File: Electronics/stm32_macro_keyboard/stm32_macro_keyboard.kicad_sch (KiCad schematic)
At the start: 26 parts, among them SW1 SW_SPDT, U1 STM32F072CBTx

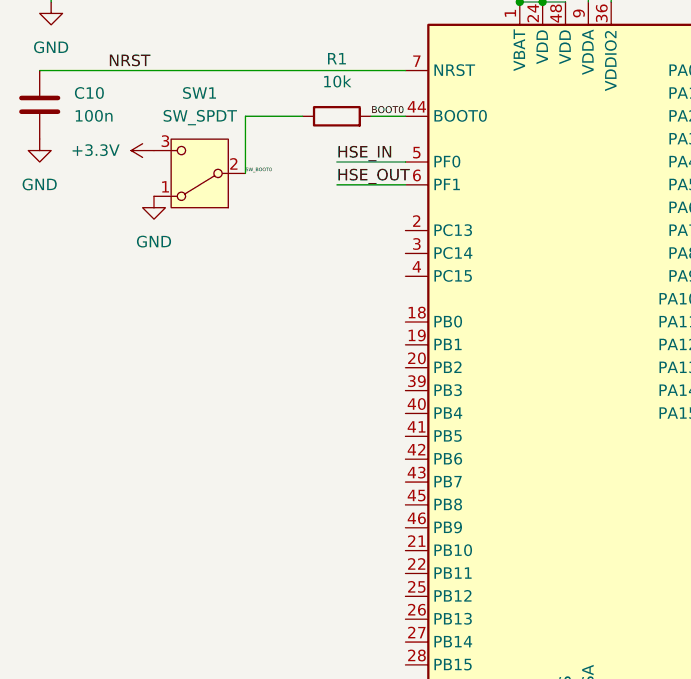
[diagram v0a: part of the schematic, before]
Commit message: Add 16 MHz HSE crystal oscillator circuit
- Add Y1 (Crystal_GND24) 16 MHz crystal on PF0/PF1 (HSE_IN/HSE_OUT)
- Add C11 and C12 (10pF) load capacitors for crystal oscillator
- Add GND connection for crystal ground pins
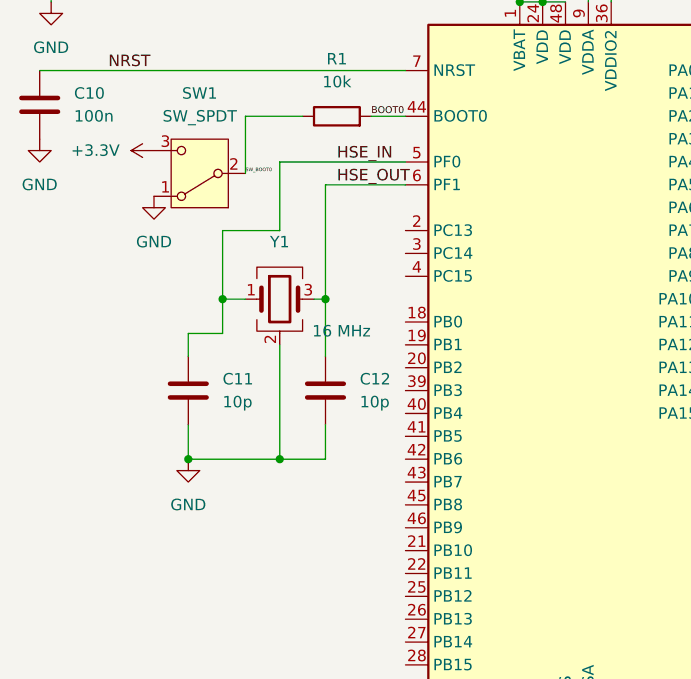
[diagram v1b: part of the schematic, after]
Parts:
- added C11, C12: 10p, symbol Device:C
- added Y1: 16 MHz, symbol Device:Crystal_GND24
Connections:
- net GND: now also C11.2, C12.2, Y1.2 (G), Y1.4 (G)
- net HSE_IN: now also C11.1, Y1.1
- net HSE_OUT: now also C12.1, Y1.3

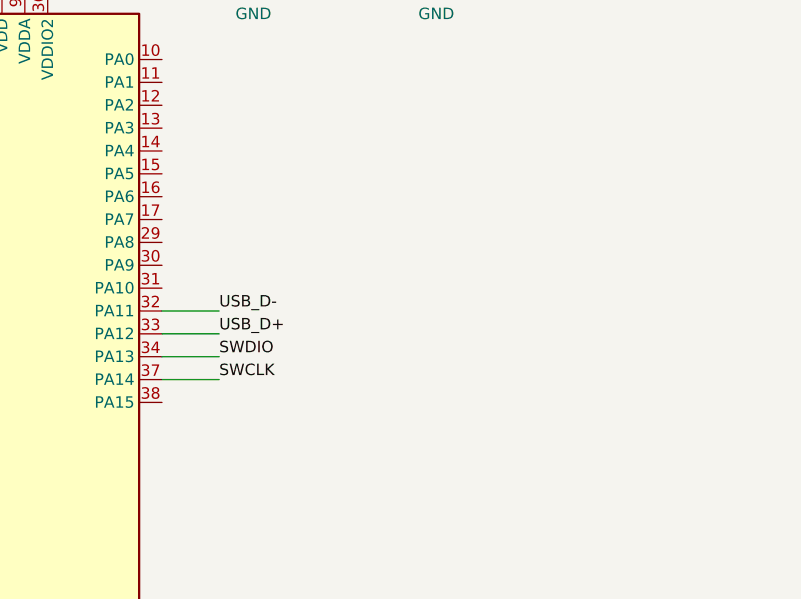
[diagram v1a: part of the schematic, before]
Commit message: Add USB Micro B connector (J1) with power and data connections
- Add J1 (USB_B_Micro) connector symbol
- Connect D- and D+ to USB_D-/USB_D+ nets on PA11/PA12
- Connect VBUS to VBUS power rail and GND pin to GND
- Mark ID and Shield pins as no-connect
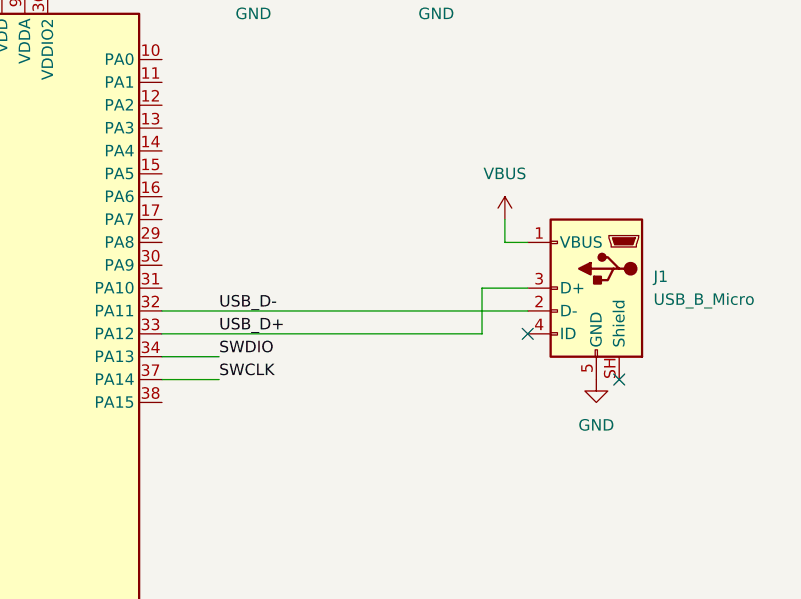
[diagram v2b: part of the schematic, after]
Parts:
- added J1: USB_B_Micro, symbol Connector:USB_B_Micro
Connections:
- net GND: now also J1.5 (GND)
- net USB_D+: now also J1.3 (D+)
- net USB_D-: now also J1.2 (D-)
- new net VBUS: J1.1 (VBUS)
- no-connect marks 0 -> 2

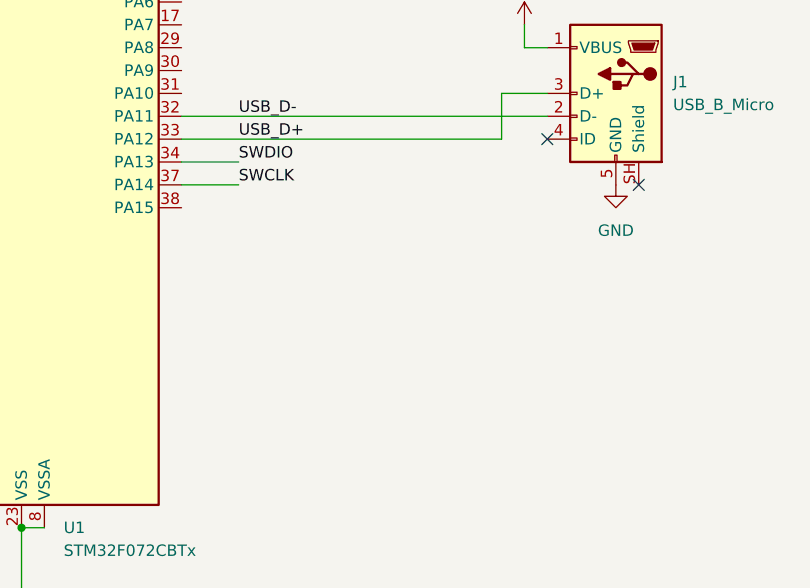
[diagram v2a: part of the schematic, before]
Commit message: Add SWD debug header (J2) and power symbols to schematic
Add a 4-pin connector J2 for SWD debug access with +3.3V and GND power
symbols. Route MCU SWD signals (SWDIO/SWCLK) to the new header via wires.
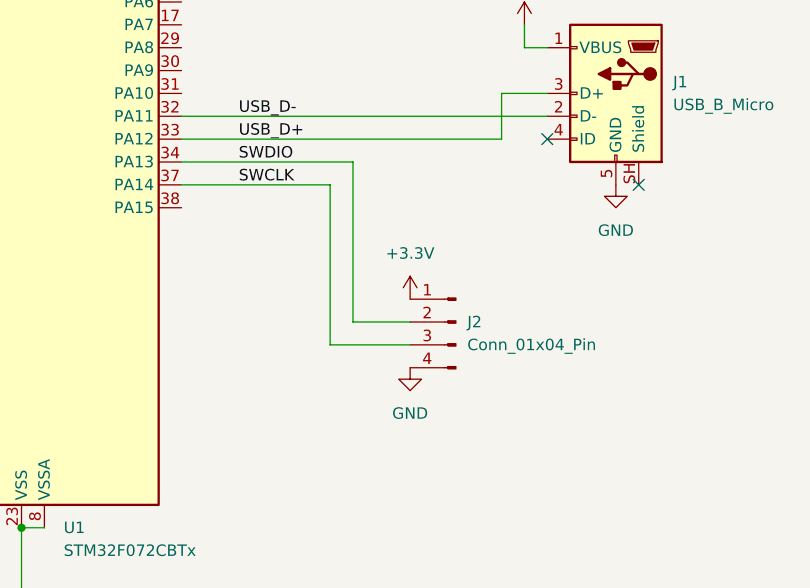
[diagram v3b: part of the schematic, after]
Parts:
- added J2: Conn_01x04_Pin, symbol Connector:Conn_01x04_Pin
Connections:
- net +3.3V: now also J2.1 (Pin_1)
- net GND: now also J2.4 (Pin_4)
- net SWCLK: now also J2.3 (Pin_3)
- net SWDIO: now also J2.2 (Pin_2)

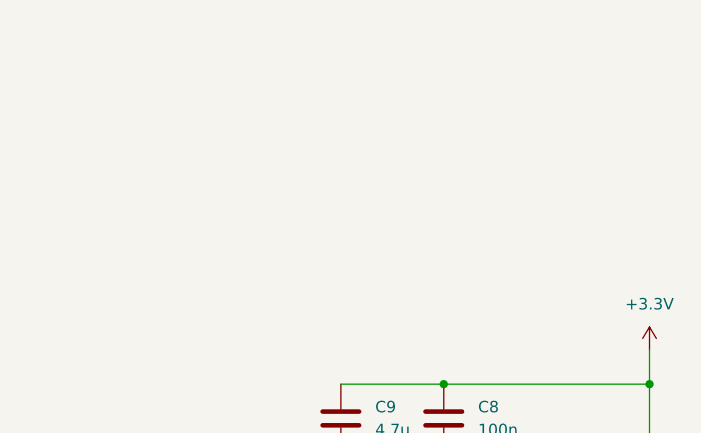
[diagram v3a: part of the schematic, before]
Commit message: Add 3.3V LDO power regulation circuit to schematic
Adds the full USB 5V → 3.3V power supply sub-circuit required to power
the STM32F072 MCU from the USB bus:

- U2 (AMS1117-3.3, SOT-223): LDO regulator converting VBUS (5V) to
  +3.3V. Chosen for its wide availability, 1A output capability, and
  simple 3-pin SOT-223 footprint that is easy to hand-solder.
- C13, C14 (22µF each): Bulk input and output bypass capacitors on the
  LDO, as recommended by the AMS1117 datasheet to ensure stability and
  suppress switching noise on the regulated rail.
- D7 (LED) + R2 (1.5kΩ): Power-on indicator LED. R2 limits current to
  ~2mA from the 3.3V rail ((3.3V - 2V_f) / 1500Ω ≈ 0.9mA), keeping
  total board current well within the SYS-02 ≤100mA USB budget.
- VBUS, +3.3V, GND power symbols and all connecting wires/junctions
  for the new sub-circuit added.

Completes the HW-02 power distribution requirement. Schematic now has
all major power supply components; remaining work is the 6-key switch
matrix, ESD protection on USB D+/D−, and PCB routing.
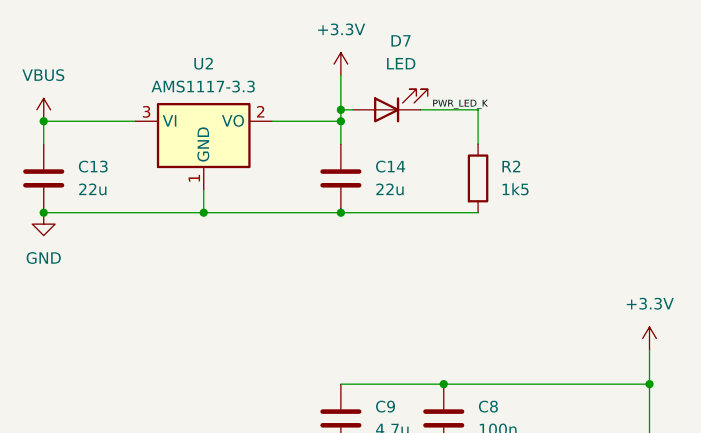
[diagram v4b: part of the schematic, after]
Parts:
- added C13, C14: 22u, symbol Device:C
- added D7: LED, symbol Device:LED
- added R2: 1k5, symbol Device:R
- added U2: AMS1117-3.3, Package_TO_SOT_SMD:SOT-223-3_TabPin2, symbol Regulator_Linear:AMS1117-3.3
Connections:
- net +3.3V: now also C14.1, D7.2 (A), U2.2 (VO)
- net GND: now also C13.2, C14.2, R2.2, U2.1 (GND)
- net VBUS: now also C13.1, U2.3 (VI)
- new net PWR_LED_K: D7.1 (K), R2.1

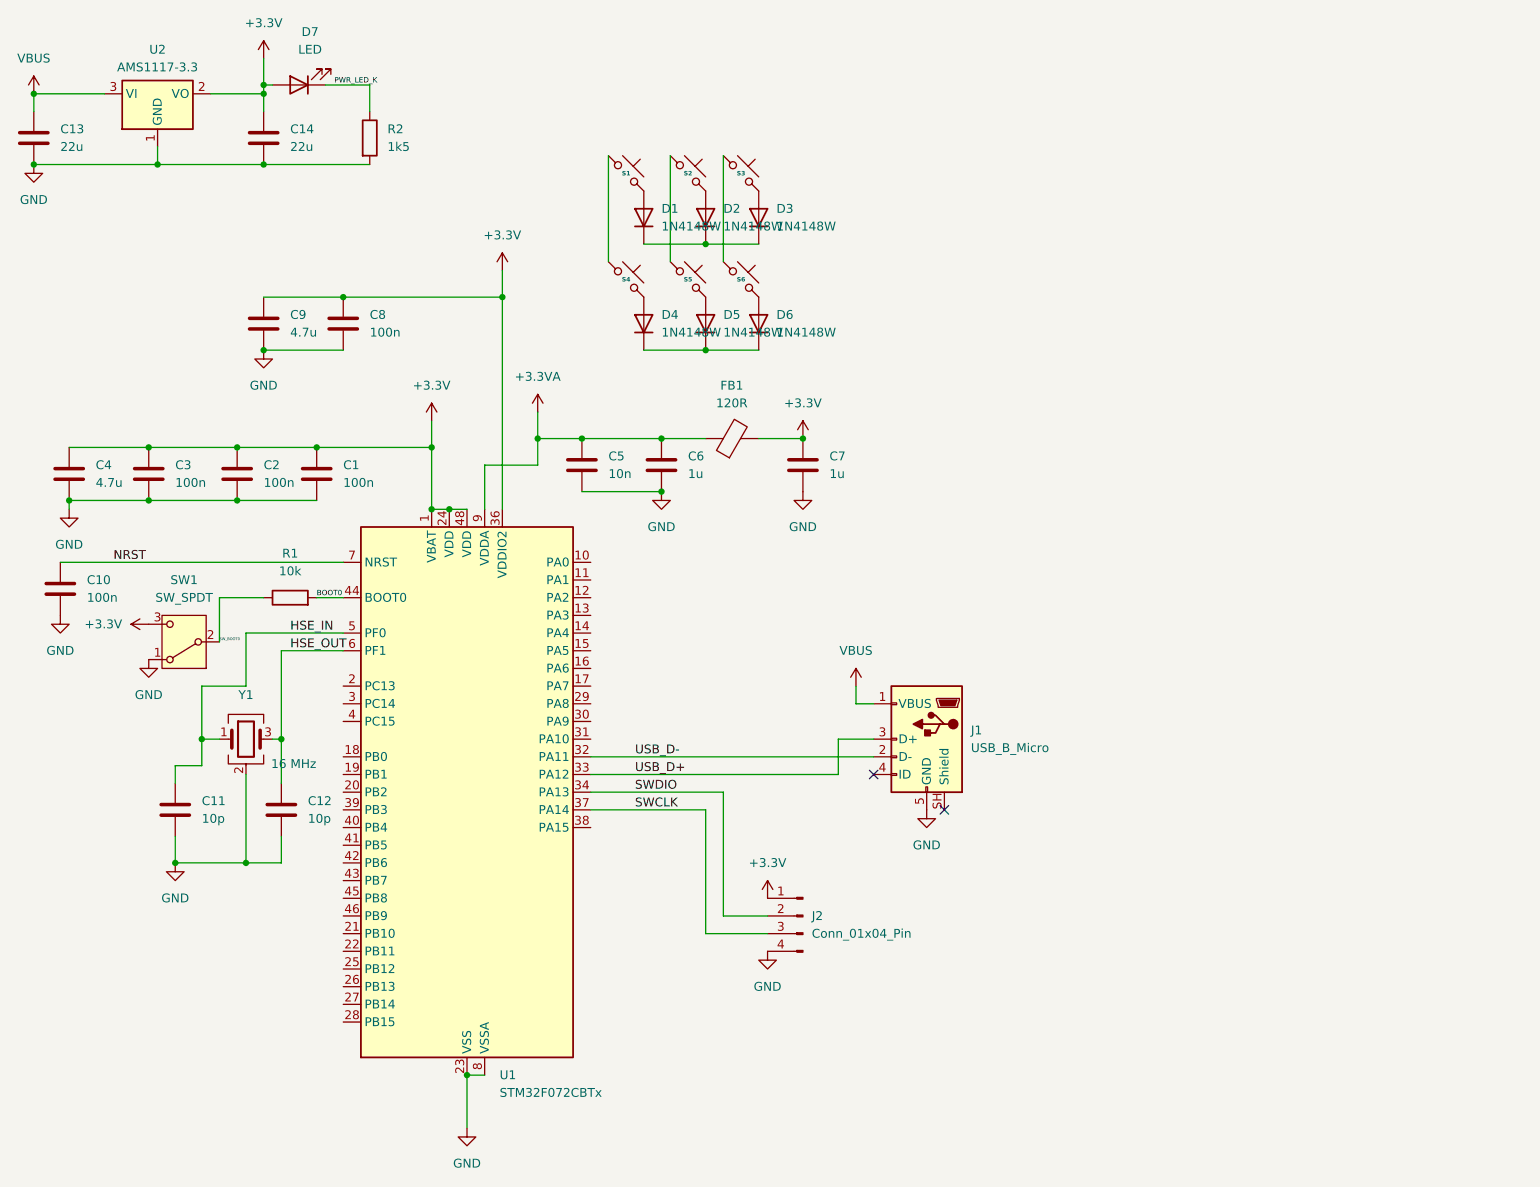
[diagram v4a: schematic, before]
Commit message: Add schematic images, begin PCB layout, and configure GPIO key matrix pins
Electronics:
- Added Electronics/img/ with a 3D PCB render (PNG) and schematic export (SVG)
  for use in the README and project documentation
- Expanded kicad_pcb from a blank stub to a full board definition with layer
  stack, design rules, net classes, and initial component placement — PCB
  layout and routing now in active progress
- Updated kicad_sch with schematic additions; wiring is complete, cosmetic
  clean-up of the schematic still pending
- Updated kicad_pro to reflect current KiCAD project state

Firmware / CubeMX:
- Configured PA3, PA4, PA5, PA6, PA7 as locked GPIO outputs in macropad.ioc
  to represent the 5 key-matrix column drive lines (S1–S5 scan GPIOs)
- Added MX_GPIO_Init and MX_USB_PCD_Init to the CubeMX function list,
  aligning the IOC with the intended peripheral initialisation order

README:
- Replaced stale placeholder comments with actual embedded images
- Added inline status captions: "PCB layout and routing in progress" under
  the 3D render, and "Wiring is completed — schematic still needs to be made
  neat and tidy" under the schematic
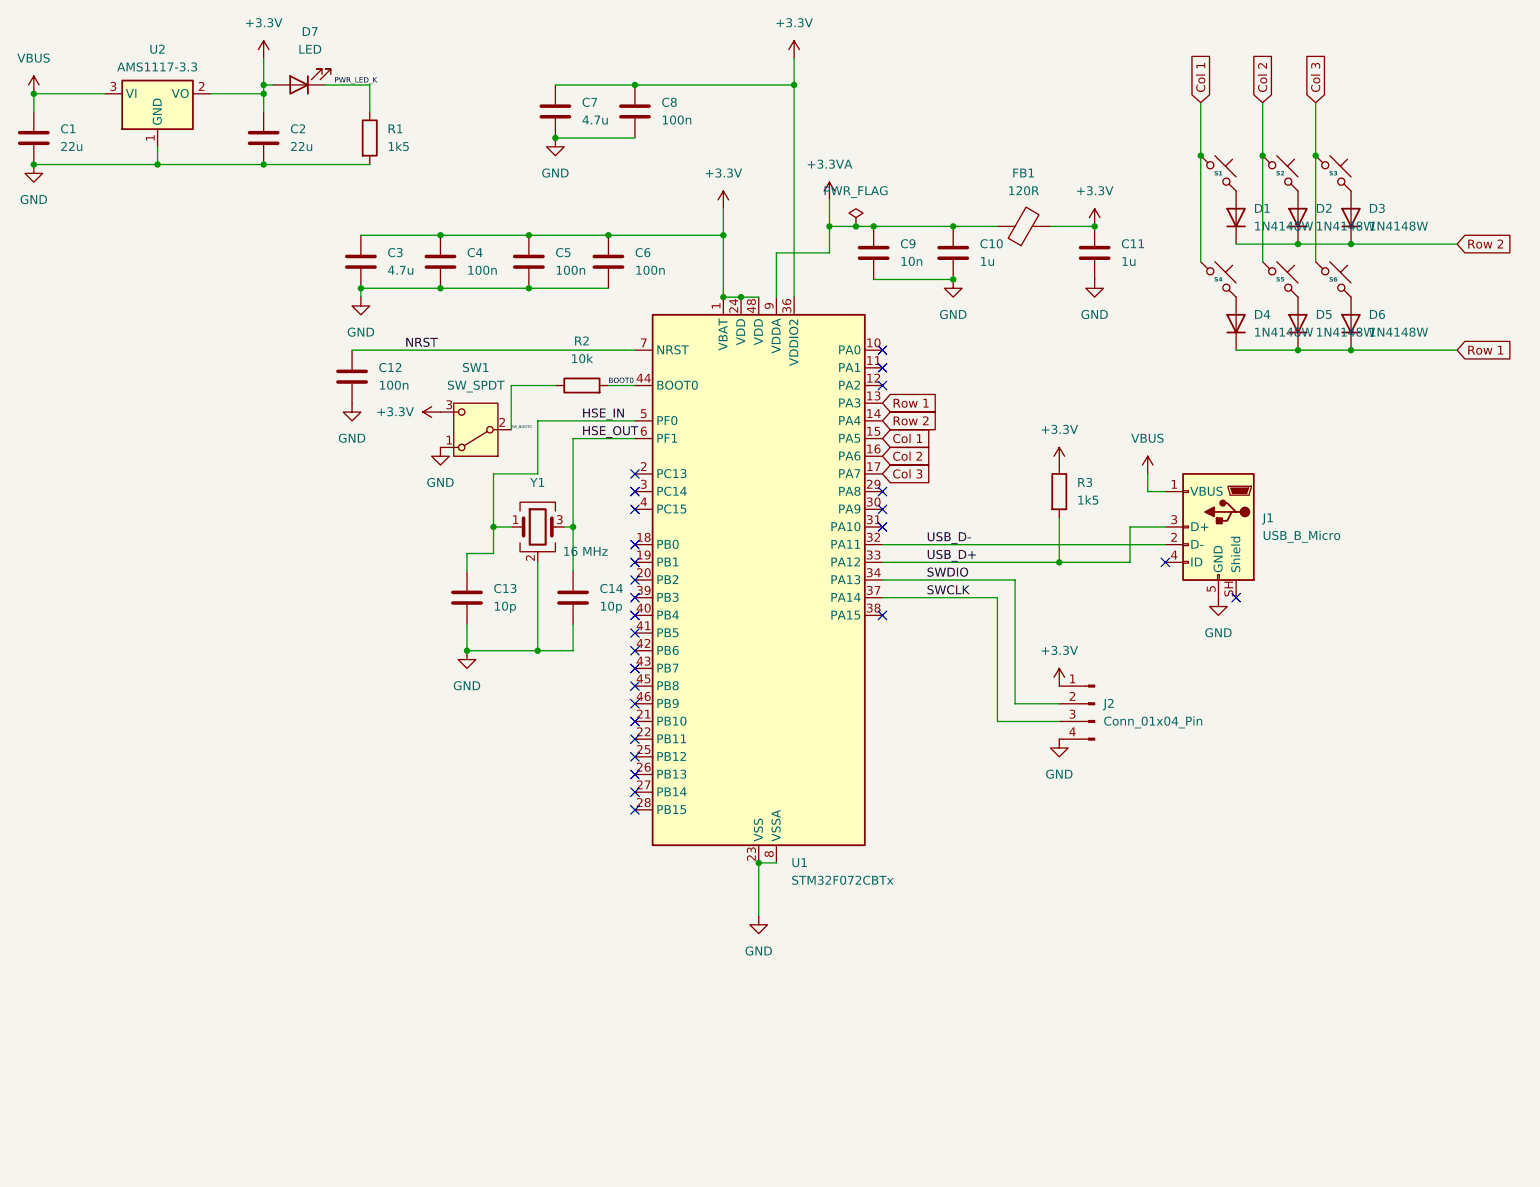
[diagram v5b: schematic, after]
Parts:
- added R3: 1k5, Resistor_SMD:R_0402_1005Metric, symbol Device:R
- C1: renamed from C13; footprint (none) -> Capacitor_SMD:C_0805_2012Metric
- C10: renamed from C6; footprint (none) -> Capacitor_SMD:C_0402_1005Metric
- C11: renamed from C7; footprint (none) -> Capacitor_SMD:C_0402_1005Metric
- C12: renamed from C10; footprint (none) -> Capacitor_SMD:C_0402_1005Metric
- C13: renamed from C11; footprint (none) -> Capacitor_SMD:C_0402_1005Metric
- C14: renamed from C12; footprint (none) -> Capacitor_SMD:C_0402_1005Metric
- C2: renamed from C14; footprint (none) -> Capacitor_SMD:C_0805_2012Metric
- C3: renamed from C4; footprint (none) -> Capacitor_SMD:C_0603_1608Metric
- C4: renamed from C3; footprint (none) -> Capacitor_SMD:C_0402_1005Metric
- C5: renamed from C2; footprint (none) -> Capacitor_SMD:C_0402_1005Metric
- C6: renamed from C1; footprint (none) -> Capacitor_SMD:C_0402_1005Metric
- C7: renamed from C9; footprint (none) -> Capacitor_SMD:C_0603_1608Metric
- C8: footprint (none) -> Capacitor_SMD:C_0402_1005Metric
- C9: renamed from C5; footprint (none) -> Capacitor_SMD:C_0402_1005Metric
- D7: footprint (none) -> LED_SMD:LED_0603_1608Metric
- FB1: footprint (none) -> Inductor_SMD:L_0603_1608Metric
- J1: footprint (none) -> Connector_USB:USB_Micro-B_Wuerth_629105150521
- J2: footprint (none) -> Connector_PinHeader_2.54mm:PinHeader_1x04_P2.54mm_Vertical
- R1: renamed from R2; footprint (none) -> Resistor_SMD:R_0402_1005Metric
- R2: renamed from R1; footprint (none) -> Resistor_SMD:R_0402_1005Metric
- S1, S2, S3, S4, S5, S6: footprint (none) -> ScottoKeebs_MX:MX_PCB_2.50u
- SW1: footprint (none) -> Button_Switch_SMD:SW_SPDT_PCM12
- Y1: footprint (none) -> Crystal:Crystal_SMD_3225-4Pin_3.2x2.5mm
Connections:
- net +3.3V: now also R3.1
- net USB_D+: now also R3.2
- net Row 1: now reaches D4.1 (K), D5.1 (K), D6.1 (K)
- net Row 1: now also U1.13 (PA3)
- net Row 2: now reaches D1.1 (K), D2.1 (K), D3.1 (K)
- net Row 2: now also U1.14 (PA4)
- net Col 1: now reaches S1.1, S4.1
- net Col 1: now also U1.15 (PA5)
- net Col 2: now reaches U1.16 (PA6)
- net Col 2: now also S2.1, S5.1
- net Col 3: now reaches U1.17 (PA7)
- net Col 3: now also S3.1, S6.1
- no-connect marks 2 -> 28
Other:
- moved on the sheet: C10, C11, C12, C13, C14, C3, C4, C5, C6, C7, C8, C9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
